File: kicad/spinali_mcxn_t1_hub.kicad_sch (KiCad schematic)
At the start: 0 parts

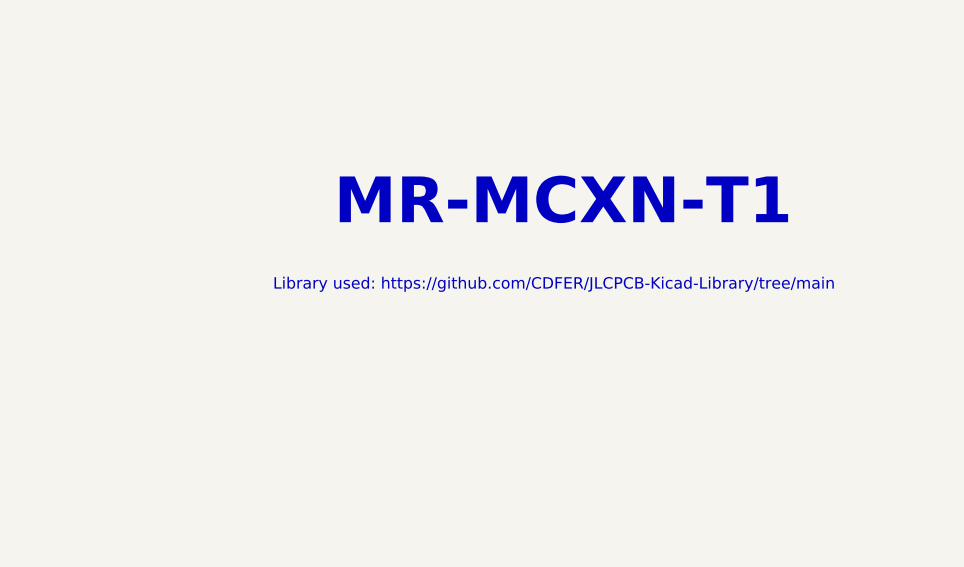
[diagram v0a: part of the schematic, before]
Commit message: Updated MR-MCXN-T1 hub to production version X1
- Populated I3C 10k pull-up resistors, R16, R17, R18 and R19
- Updated page information and revision number to X1
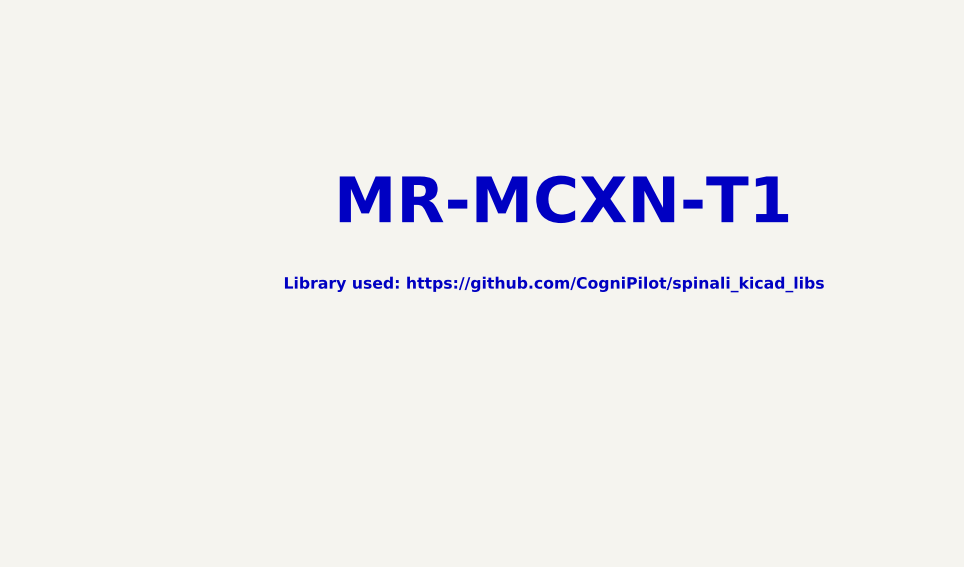
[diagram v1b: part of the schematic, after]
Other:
- note added: "Library used: https://github.com/CogniPilot/spinali_kicad_libs"
- note removed: "Library used: https://github.com/CDFER/JLCPCB-Kicad-Library/tree/main"
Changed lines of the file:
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@@
 	(title_block
 		(title "MR-MCXN-T1")
-		(date "2025-03-28")
-		(rev "X0")
+		(date "2026-07-24")
+		(rev "X1")
 		(company "NXP SEMICONDUCTORS B.V.")
-		(comment 3 "DESIGNER: YOURI TILS")
-		(comment 4 "CTO SYSTEM INNOVATIONS / MOBILE ROBOTICS DOMAIN")
+		(comment 1 "DESIGNER: YOURI TILS")
+		(comment 2 "CTO SYSTEM INNOVATIONS / MOBILE ROBOTICS DOMAIN")
 	)
 	(text "MR-MCXN-T1"
@@
 		)
 	)
-	(text "Library used: https://github.com/CDFER/JLCPCB-Kicad-Library/tree/main"
+	(text "Library used: https://github.com/CogniPilot/spinali_kicad_libs"
 		(exclude_from_sim no)
 		(at 153.924 100.33 0)
@@
 			(font
 				(size 1.27 1.27)
+				(thickness 0.381)
+				(bold yes)
 			)
 		)

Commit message: MR-MCXN-T1 Rev A Production
- Added Rev A in schematic and layout
- Updated footprints
- Succesfull DRC

Signed-off-by: Youri Tils <youri.tils@nxp.com>
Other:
- company: NXP SEMICONDUCTORS B.V. -> ${COMPANY}
- title: MR-MCXN-T1 -> ${TITLE}
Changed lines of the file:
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@@
 	(paper "A4")
 	(title_block
-		(title "MR-MCXN-T1")
-		(date "2026-07-27")
-		(rev "X1")
-		(company "NXP SEMICONDUCTORS B.V.")
-		(comment 1 "DESIGNER: YOURI TILS")
-		(comment 2 "CTO SYSTEM INNOVATIONS / MOBILE ROBOTICS DOMAIN")
+		(title "${TITLE}")
+		(date "2026-08-24")
+		(rev "${BOARD_REV}")
+		(company "${COMPANY}")
+		(comment 1 "DESIGNER: ${DESIGNER}")
+		(comment 2 "${DEPARTMENT}")
+		(comment 3 "REVIEWED BY: ${REVIEWER}")
 	)
 	(text "MR-MCXN-T1"

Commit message: Add block diagram
added new sheet with simple block diagram. No changes to actual schematic or layout.
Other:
- added sheet Block Diagram (block_diagram_sch.kicad_sch)
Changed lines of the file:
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@@
+	)
+	(sheet
+		(at 50.8 39.37)
+		(size 40.64 5.08)
+		(exclude_from_sim no)
+		(in_bom yes)
+		(on_board yes)
+		(dnp no)
+		(fields_autoplaced yes)
+		(stroke
+			(width 0.1524)
+			(type solid)
+		)
+		(fill
+			(color 0 0 0 0.0000)
+		)
+		(property "Sheetname" "Block Diagram"
+			(at 50.8 38.6584 0)
+			(effects
+				(font
+					(size 1.27 1.27)
+				)
+				(justify left bottom)
+			)
+		)
+		(property "Sheetfile" "block_diagram_sch.kicad_sch"
+			(at 50.8 45.0346 0)
+			(effects
+				(font
+					(size 1.27 1.27)
+				)
+				(justify left top)
+			)
+		)
+		(instances
+			(project "spinali_mcxn_t1_hub"
+				(path "/8b469ec1-e800-4d46-8a32-95d77ceae6db"
+					(page "10")
+				)
+			)
+		)
 	)
 	(sheet
